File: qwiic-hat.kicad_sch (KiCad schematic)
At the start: 3 parts, among them J1 Conn_02x20_Odd_Even, J2 Conn_01x04_Male, J3 Conn_01x04_Male

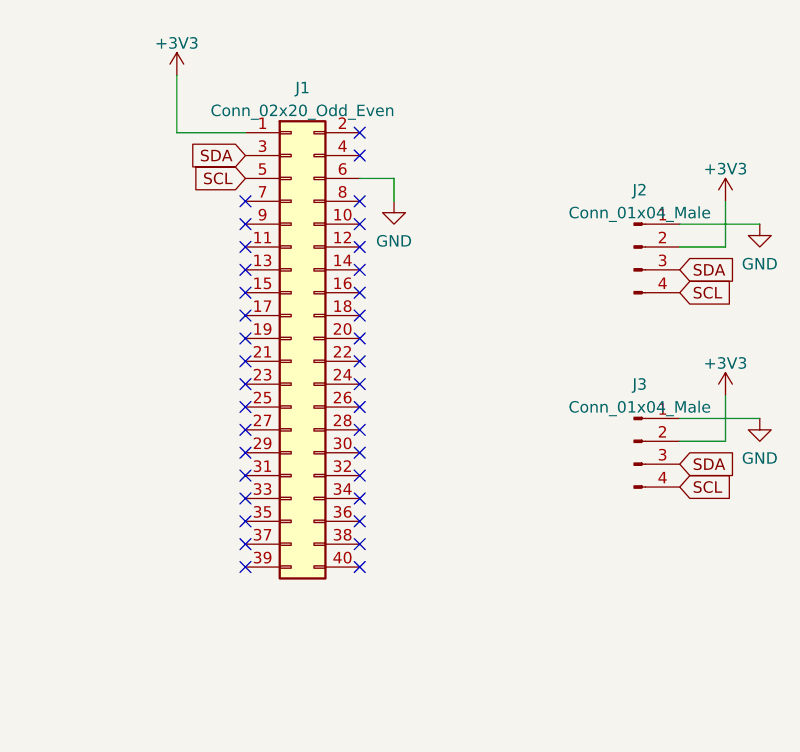
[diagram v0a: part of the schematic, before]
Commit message: added a 5v 3-pin header
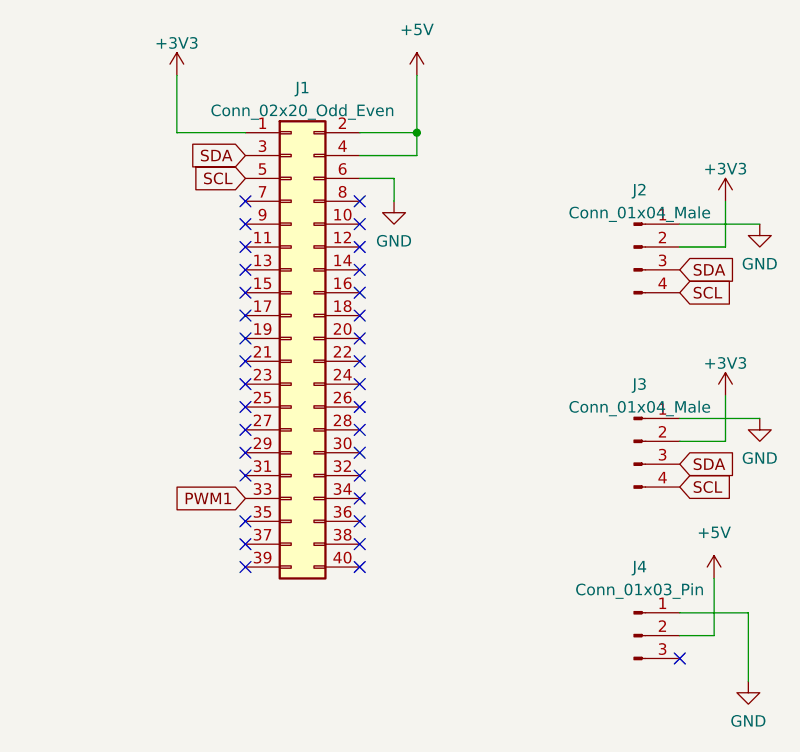
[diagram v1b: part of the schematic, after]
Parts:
- added J4: Conn_01x03_Pin, Connector:FanPinHeader_1x03_P2.54mm_Vertical, symbol Connector:Conn_01x03_Pin
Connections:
- net GND: now also J4.1 (Pin_1)
- net +5V: now reaches J1.2 (Pin_2)
- net +5V: now also J1.4 (Pin_4), J4.2 (Pin_2)
- net PWM1: now reaches J1.33 (Pin_33)
- no-connect marks 37 -> 35
